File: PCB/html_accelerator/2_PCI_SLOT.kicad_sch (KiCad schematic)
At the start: 6 parts, among them J2 Bus_PCI_Express_x8, J3 PCIexpress_bracket

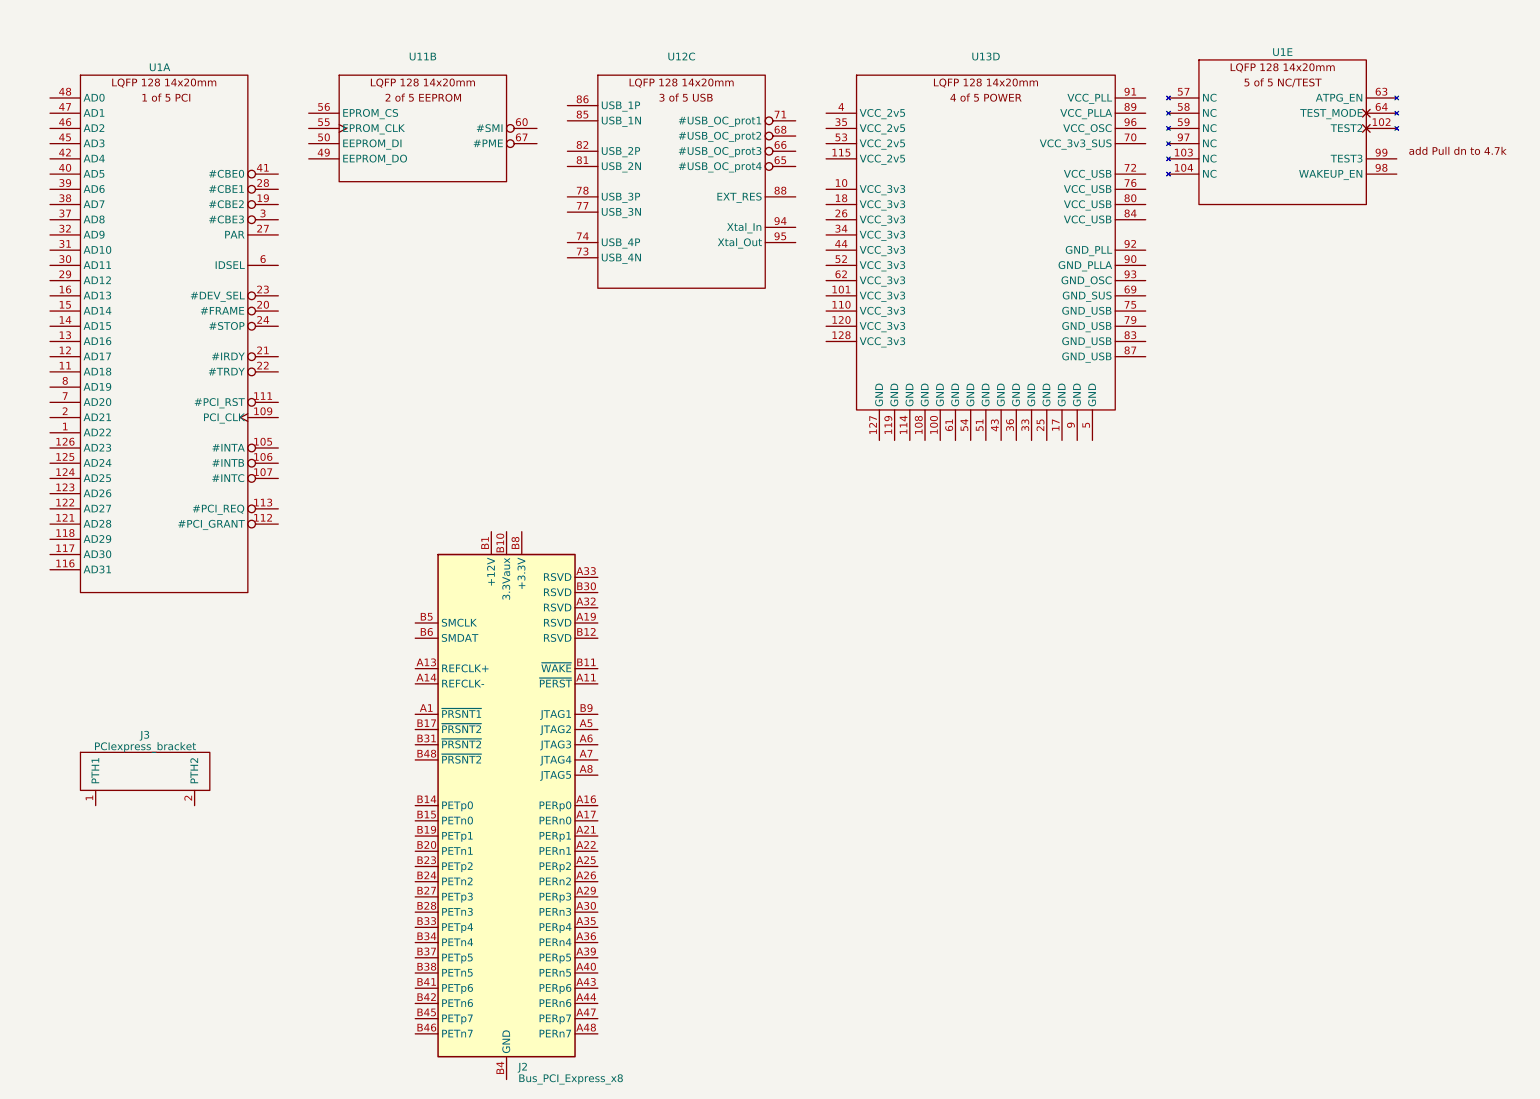
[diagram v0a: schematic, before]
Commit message: Update to MCS9990 for PCIE direct to USB
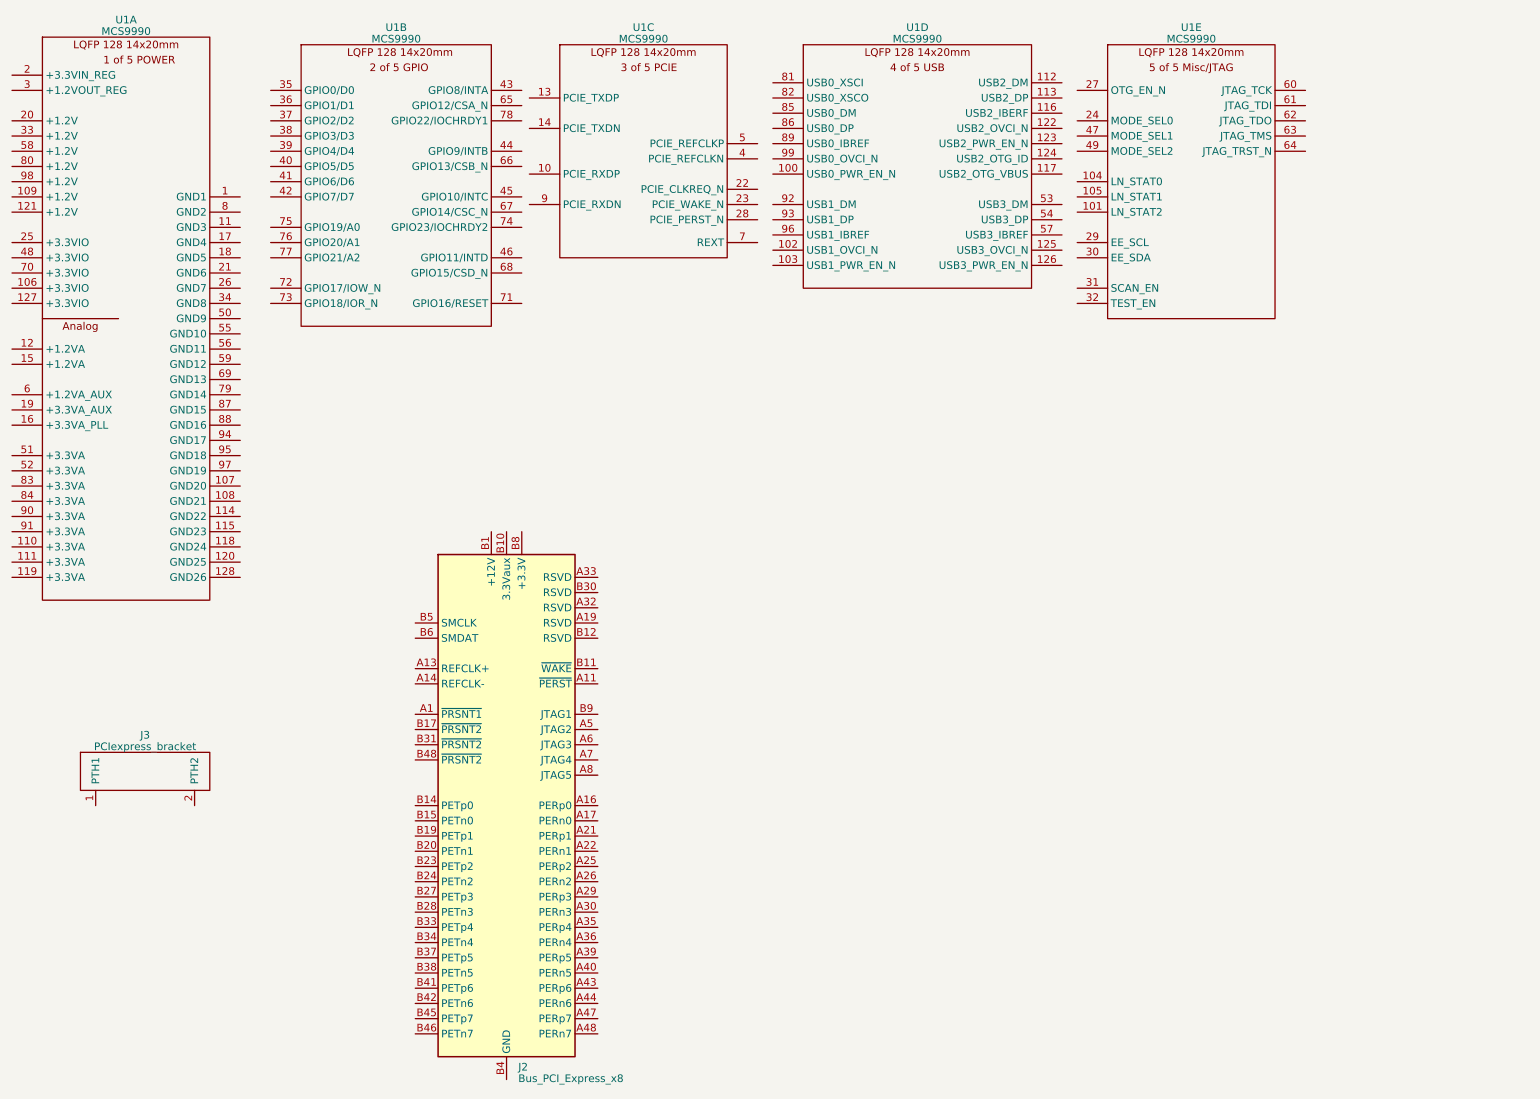
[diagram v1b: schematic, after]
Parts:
- removed U1, U11, U12, U13: ~, Package_QFP:LQFP-128_14x20mm_P0.5mm, symbol html_accel_Symbols:VT6212
- added U1: MCS9990, Package_QFP:LQFP-128_14x14mm_P0.4mm, symbol html_accel_Symbols:MCS9990
